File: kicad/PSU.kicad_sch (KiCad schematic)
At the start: 28 parts

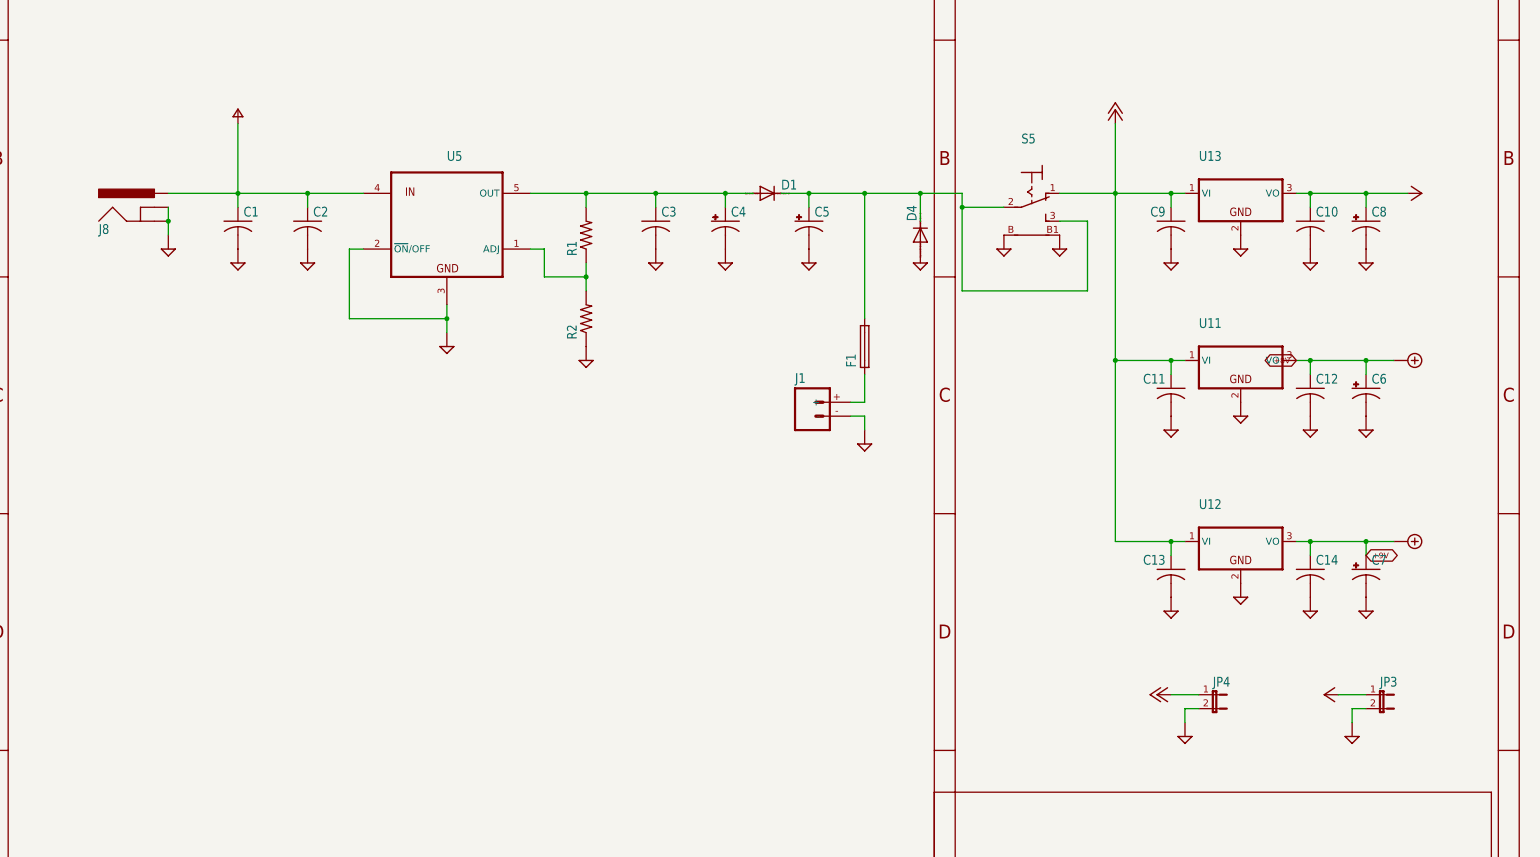
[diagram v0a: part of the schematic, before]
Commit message: Conversion of display print to KiCad components; still attached to main board
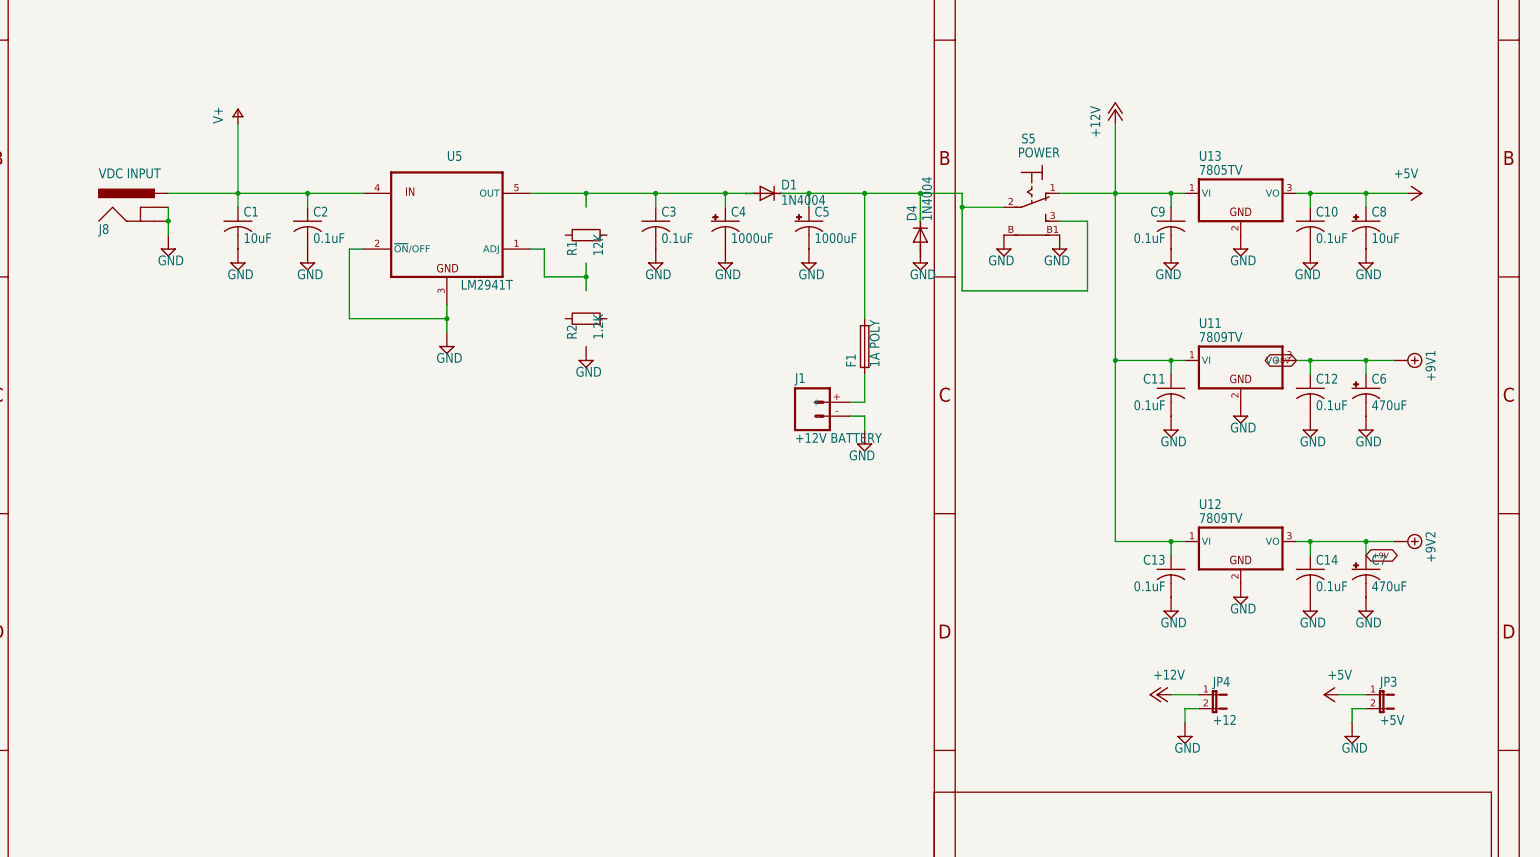
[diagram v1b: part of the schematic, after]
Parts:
- C1: value (none) -> 10uF; footprint (none) -> mk312:C050-024X044
- C10, C11, C12, C13, C14, C2, C3, C9: value (none) -> 0.1uF; footprint (none) -> mk312:C025-024X044
- C4, C5: value (none) -> 1000uF; footprint (none) -> mk312:E5-10,5
- C6, C7: value (none) -> 470uF; footprint (none) -> mk312:E3,5-8
- C8: value (none) -> 10uF; footprint (none) -> mk312:E2,5-7
- D1, D4: value (none) -> 1N4004; footprint (none) -> mk312:DO41-10
- F1: value (none) -> 1A POLY; footprint (none) -> mk312:LITTLEFUSE
- J1: value (none) -> +12V BATTERY; footprint (none) -> mk312:DEANS
- J8: value (none) -> VDC INPUT; footprint (none) -> mk312:POWER_JACK_SLOT
- JP3: value (none) -> +5V; footprint (none) -> mk312:JP1
- JP4: value (none) -> +12; footprint (none) -> mk312:JP1
- R1: value (none) -> 12K; footprint (none) -> mk312:0207_10; symbol mk312-eagle-import:R-US_0207/10 -> Device:R
- R2: value (none) -> 1.2K; footprint (none) -> mk312:0207_10; symbol mk312-eagle-import:R-US_0207/10 -> Device:R
- S5: value (none) -> POWER; footprint (none) -> mk312:LPV-1
- U11, U12: value (none) -> 7809TV; footprint (none) -> mk312:TO220V
- U13: value (none) -> 7805TV; footprint (none) -> mk312:TO220V
- U5: value (none) -> LM2941T; footprint (none) -> mk312:TO220-5
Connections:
- net GND: no longer R2.1
- net at C3.1, C4.+, D1.A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: no longer R1.2
- now unconnected: R1.1, R2.2, U5.1 (ADJ)
